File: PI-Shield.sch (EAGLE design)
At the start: 77 parts, among them IC1 PCF8574T, J10 T2I, J11 T2I, J12 T2I, J13 DF13-4P-1.25DSA, J14 DF13-4P-1.25DSA, J15 DF13-4P-1.25DSA, Q1 220mA/50V/3.5Ω, Q2 220mA/50V/3.5Ω, Q3 220mA/50V/3.5Ω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

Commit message: v2 Changes
Would like to formally apologize for the routing of the GPIO on the bottom of the board. It was necessary, unfortunately.
Changes: [Removed expander, added LED and Header Labels, really shitty routing.]
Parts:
- removed IC1: PCF8574T, micro-philips:PCF8574T
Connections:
- net 3V3: no longer IC1.VDD
- net GND: no longer IC1.A0, IC1.A1, IC1.A2, IC1.VSS
- net GPIO1: now also U$8.GPIO18; no longer IC1.P0
- net GPIO2: now also U$8.GPIO23; no longer IC1.P1
- net GPIO3: now also U$8.GPIO24; no longer IC1.P2
- net GPIO4: now also U$8.GPIO25; no longer IC1.P3
- net GPIO5: now also U$8.GPIO12; no longer IC1.P4
- net GPIO6: now also U$8.GPIO21; no longer IC1.P5
- net SCL: no longer IC1.SCL
- net SDA: no longer IC1.SDA
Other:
- note removed: "(address inputs)"
- note removed: "(used in place of the STM from last year)"
- note removed: "I/O Expander"
- note removed: "PCAL9554CPWJ"
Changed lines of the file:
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@@
 <part name="FRAME6" library="SparkFun-Aesthetics" library_urn="urn:adsk.eagle:library:507" deviceset="FRAME-A4L" device=""/>
 <part name="U3" library="ULN2003V12" deviceset="ULN2003V12" device=""/>
-<part name="IC1" library="micro-philips" library_urn="urn:adsk.eagle:library:290" deviceset="PCF8574" device="T" package3d_urn="urn:adsk.eagle:package:20172/1"/>
-<part name="SUPPLY1" library="supply2" library_urn="urn:adsk.eagle:library:372" deviceset="GND" device=""/>
 <part name="C15" library="SparkFun-Capacitors" library_urn="urn:adsk.eagle:library:510" deviceset="47UF-POLAR" device="-PANASONIC_D-35V-20%" package3d_urn="urn:adsk.eagle:package:37420/1" value="47uF"/>
 <part name="U$3" library="PI-SHIELD, Solenoid-Backplane" deviceset="6X_CONN" device=""/>
@@
 <wire x1="231.14" y1="149.86" x2="238.76" y2="149.86" width="0.1524" layer="91"/>
 <label x="233.68" y="149.86" size="1.778" layer="95"/>
+</segment>
+</net>
+<net name="GPIO1" class="0">
+<segment>
+<pinref part="U$8" gate="G$1" pin="GPIO18"/>
+<wire x1="25.4" y1="43.18" x2="20.32" y2="43.18" width="0.1524" layer="91"/>
+<label x="20.32" y="43.18" size="1.778" layer="95" rot="R180" xref="yes"/>
+</segment>
+</net>
+<net name="GPIO2" class="0">
+<segment>
+<pinref part="U$8" gate="G$1" pin="GPIO23"/>
+<wire x1="25.4" y1="53.34" x2="20.32" y2="53.34" width="0.1524" layer="91"/>
+<label x="20.32" y="53.34" size="1.778" layer="95" rot="R180" xref="yes"/>
+</segment>
+</net>
+<net name="GPIO3" class="0">
+<segment>
+<pinref part="U$8" gate="G$1" pin="GPIO24"/>
+<wire x1="25.4" y1="58.42" x2="20.32" y2="58.42" width="0.1524" layer="91"/>
+<label x="20.32" y="58.42" size="1.778" layer="95" rot="R180" xref="yes"/>
+</segment>
+</net>
+<net name="GPIO4" class="0">
+<segment>
+<pinref part="U$8" gate="G$1" pin="GPIO25"/>
+<wire x1="25.4" y1="68.58" x2="20.32" y2="68.58" width="0.1524" layer="91"/>
+<label x="20.32" y="68.58" size="1.778" layer="95" rot="R180" xref="yes"/>
+</segment>
+</net>
+<net name="GPIO5" class="0">
+<segment>
+<pinref part="U$8" gate="G$1" pin="GPIO12"/>
+<wire x1="25.4" y1="93.98" x2="20.32" y2="93.98" width="0.1524" layer="91"/>
+<label x="20.32" y="93.98" size="1.778" layer="95" rot="R180" xref="yes"/>
+</segment>
+</net>
+<net name="GPIO6" class="0">
+<segment>
+<pinref part="U$8" gate="G$1" pin="GPIO21"/>
+<wire x1="25.4" y1="114.3" x2="20.32" y2="114.3" width="0.1524" layer="91"/>
+<label x="20.32" y="114.3" size="1.778" layer="95" rot="R180" xref="yes"/>
 </segment>
 </net>
@@
 <text x="53.34" y="157.48" size="6.4516" layer="91">NPN Array</text>
 <text x="180.34" y="149.86" size="6.4516" layer="91">Connectors</text>
-<text x="142.24" y="86.36" size="1.778" layer="91">I/O Expander</text>
-<text x="137.16" y="43.18" size="1.778" layer="91">(used in place of the STM
-from last year)</text>
-<text x="139.7" y="86.36" size="1.778" layer="91">
-PCAL9554CPWJ
-</text>
-<text x="119.38" y="53.34" size="1.778" layer="91">(address inputs)</text>
 <text x="33.02" y="45.72" size="1.778" layer="91">decoupling cap for solenoids</text>
 <text x="33.02" y="48.26" size="1.778" layer="91">UZ476M035HEHTA</text>
@@
 </instance>
 <instance part="U3" gate="G$1" x="71.12" y="116.84" smashed="yes"/>
-<instance part="IC1" gate="G$1" x="147.32" y="68.58" smashed="yes"/>
-<instance part="SUPPLY1" gate="GND" x="114.3" y="50.8" smashed="yes">
-<attribute name="VALUE" x="112.395" y="47.625" size="1.778" layer="96"/>
-</instance>
 <instance part="C15" gate="G$1" x="68.58" y="48.26" smashed="yes">
 <attribute name="NAME" x="69.596" y="48.895" size="1.778" layer="95" font="vector"/>
@@
 </segment>
 <segment>
-<pinref part="IC1" gate="G$1" pin="VSS"/>
-<wire x1="160.02" y1="53.34" x2="172.72" y2="53.34" width="0.1524" layer="91"/>
-<label x="170.18" y="53.34" size="1.778" layer="95" align="bottom-right"/>
-</segment>
-<segment>
-<pinref part="IC1" gate="G$1" pin="A2"/>
-<wire x1="137.16" y1="58.42" x2="114.3" y2="58.42" width="0.1524" layer="91"/>
-<label x="127" y="58.42" size="1.778" layer="95"/>
-<pinref part="IC1" gate="G$1" pin="A1"/>
-<wire x1="137.16" y1="60.96" x2="114.3" y2="60.96" width="0.1524" layer="91"/>
-<label x="127" y="60.96" size="1.778" layer="95"/>
-<pinref part="IC1" gate="G$1" pin="A0"/>
-<wire x1="137.16" y1="63.5" x2="114.3" y2="63.5" width="0.1524" layer="91"/>
-<label x="127" y="63.5" size="1.778" layer="95"/>
-<wire x1="114.3" y1="63.5" x2="114.3" y2="60.96" width="0.1524" layer="91"/>
-<wire x1="114.3" y1="60.96" x2="114.3" y2="58.42" width="0.1524" layer="91"/>
-<junction x="114.3" y="60.96"/>
-<wire x1="114.3" y1="58.42" x2="114.3" y2="53.34" width="0.1524" layer="91"/>
-<junction x="114.3" y="58.42"/>
-<pinref part="SUPPLY1" gate="GND" pin="GND"/>
-</segment>
-<segment>
 <wire x1="68.58" y1="43.18" x2="68.58" y2="38.1" width="0.1524" layer="91"/>
 <label x="68.58" y="35.56" size="1.778" layer="95" rot="R90"/>
@@
 <pinref part="U3" gate="G$1" pin="IN1"/>
 </segment>
-<segment>
-<pinref part="IC1" gate="G$1" pin="P0"/>
-<wire x1="160.02" y1="76.2" x2="172.72" y2="76.2" width="0.1524" layer="91"/>
-<label x="170.18" y="76.2" size="1.778" layer="95" align="bottom-right"/>
-</segment>
 </net>
 <net name="GPIO6" class="0">
@@
 <pinref part="U3" gate="G$1" pin="IN6"/>
 </segment>
-<segment>
-<pinref part="IC1" gate="G$1" pin="P5"/>
-<wire x1="160.02" y1="63.5" x2="172.72" y2="63.5" width="0.1524" layer="91"/>
-<label x="170.18" y="63.5" size="1.778" layer="95" align="bottom-right"/>
-</segment>
 </net>
 <net name="GPIO5" class="0">
@@
 <pinref part="U3" gate="G$1" pin="IN5"/>
 </segment>
-<segment>
-<pinref part="IC1" gate="G$1" pin="P4"/>
-<wire x1="160.02" y1="66.04" x2="172.72" y2="66.04" width="0.1524" layer="91"/>
-<label x="170.18" y="66.04" size="1.778" layer="95" align="bottom-right"/>
-</segment>
 </net>
 <net name="GPIO4" class="0">
@@
 <pinref part="U3" gate="G$1" pin="IN4"/>
 </segment>
-<segment>
-<pinref part="IC1" gate="G$1" pin="P3"/>
-<wire x1="160.02" y1="68.58" x2="172.72" y2="68.58" width="0.1524" layer="91"/>
-<label x="170.18" y="68.58" size="1.778" layer="95" align="bottom-right"/>
-</segment>
 </net>
 <net name="GPIO3" class="0">
@@
 <pinref part="U3" gate="G$1" pin="IN3"/>
 </segment>
-<segment>
-<pinref part="IC1" gate="G$1" pin="P2"/>
-<wire x1="160.02" y1="71.12" x2="172.72" y2="71.12" width="0.1524" layer="91"/>
-<label x="170.18" y="71.12" size="1.778" layer="95" align="bottom-right"/>
-</segment>
 </net>
 <net name="GPIO2" class="0">
@@
 <pinref part="U3" gate="G$1" pin="IN2"/>
 </segment>
-<segment>
-<pinref part="IC1" gate="G$1" pin="P1"/>
-<wire x1="160.02" y1="73.66" x2="172.72" y2="73.66" width="0.1524" layer="91"/>
-<label x="170.18" y="73.66" size="1.778" layer="95" align="bottom-right"/>
-</segment>
-</net>
-<net name="SCL" class="0">
-<segment>
-<pinref part="IC1" gate="G$1" pin="SCL"/>
-<wire x1="137.16" y1="68.58" x2="124.46" y2="68.58" width="0.1524" layer="91"/>
-<label x="127" y="68.58" size="1.778" layer="95"/>
-</segment>
-</net>
-<net name="SDA" class="0">
-<segment>
-<pinref part="IC1" gate="G$1" pin="SDA"/>
-<wire x1="137.16" y1="71.12" x2="124.46" y2="71.12" width="0.1524" layer="91"/>
-<label x="127" y="71.12" size="1.778" layer="95"/>
-</segment>
 </net>
 <net name="5V" class="2">
@@
 </net>
 <net name="3V3" class="3">
-<segment>
-<pinref part="IC1" gate="G$1" pin="VDD"/>
-<wire x1="160.02" y1="81.28" x2="172.72" y2="81.28" width="0.1524" layer="91"/>
-<label x="170.18" y="81.28" size="1.778" layer="95" align="bottom-right"/>
-</segment>
 <segment>
 <wire x1="182.88" y1="125.73" x2="195.58" y2="125.73" width="0.1524" layer="91"/>
@@
 packages will not be understood (or retained) with this version.
 </note>
-<note version="9.0" severity="warning">
-Since Version 9.0, EAGLE supports the align property for labels.
-Labels in schematic will not be understood with this version. Update EAGLE to the latest version
-for full support of labels.
-</note>
 </compatibility>

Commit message: Adjusted some labels, fixed minor errors
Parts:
- removed U$3: 6X_CONN, PI-SHIELD, Solenoid-Backplane:6X_CONN
- added U$9: 7X_CONN, PI-SHIELD, Solenoid-Backplane:7X_CONN
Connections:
- net 12V: now also U$9.13, U$9.15; no longer U$3.13, U$3.15
- net 3V3: now also U$9.23; no longer U$3.23
- net 5V: now also U$9.19; no longer U$3.19
- net CAN_H: now also U$9.1
- net CAN_L: now also U$9.2
- net GND: now also U$9.17, U$9.21; no longer U$3.17, U$3.21
- net SOL1_1: now also U$9.14; no longer U$3.14
- net SOL2_1: now also U$9.16; no longer U$3.16
- net SOL3_1: now also U$9.18; no longer U$3.18
- net SOL4_1: now also U$9.20; no longer U$3.20
- net SOL5_1: now also U$9.22; no longer U$3.22
- net SOL6_1: now also U$9.24; no longer U$3.24
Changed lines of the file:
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@@
 <?xml version="1.0" encoding="utf-8"?>
 <!DOCTYPE eagle SYSTEM "eagle.dtd">
-<eagle version="9.6.2">
+<eagle version="9.5.0">
 <drawing>
 <settings>
@@
 <setting verticaltext="up"/>
 </settings>
-<grid distance="0.1" unitdist="inch" unit="inch" style="lines" multiple="1" display="no" altdistance="0.01" altunitdist="inch" altunit="inch"/>
+<grid distance="50" unitdist="mil" unit="mil" style="lines" multiple="1" display="no" altdistance="0.01" altunitdist="inch" altunit="inch"/>
 <layers>
 <layer number="1" name="Top" color="4" fill="1" visible="no" active="no"/>
@@
 <part name="U3" library="ULN2003V12" deviceset="ULN2003V12" device=""/>
 <part name="C15" library="SparkFun-Capacitors" library_urn="urn:adsk.eagle:library:510" deviceset="47UF-POLAR" device="-PANASONIC_D-35V-20%" package3d_urn="urn:adsk.eagle:package:37420/1" value="47uF"/>
-<part name="U$3" library="PI-SHIELD, Solenoid-Backplane" deviceset="6X_CONN" device=""/>
+<part name="U$9" library="PI-SHIELD, Solenoid-Backplane" deviceset="7X_CONN" device=""/>
 </parts>
 <sheets>
@@
 <segment>
 <pinref part="U$8" gate="G$1" pin="GPIO18"/>
-<wire x1="25.4" y1="43.18" x2="20.32" y2="43.18" width="0.1524" layer="91"/>
-<label x="20.32" y="43.18" size="1.778" layer="95" rot="R180" xref="yes"/>
+<wire x1="25.4" y1="43.18" x2="19.05" y2="43.18" width="0.1524" layer="91"/>
+<label x="19.05" y="43.18" size="1.778" layer="95" rot="R180" xref="yes"/>
 </segment>
 </net>
@@
 <segment>
 <pinref part="U$8" gate="G$1" pin="GPIO23"/>
-<wire x1="25.4" y1="53.34" x2="20.32" y2="53.34" width="0.1524" layer="91"/>
-<label x="20.32" y="53.34" size="1.778" layer="95" rot="R180" xref="yes"/>
+<wire x1="25.4" y1="53.34" x2="19.05" y2="53.34" width="0.1524" layer="91"/>
+<label x="19.05" y="53.34" size="1.778" layer="95" rot="R180" xref="yes"/>
 </segment>
 </net>
@@
 <segment>
 <pinref part="U$8" gate="G$1" pin="GPIO12"/>
-<wire x1="25.4" y1="93.98" x2="20.32" y2="93.98" width="0.1524" layer="91"/>
-<label x="20.32" y="93.98" size="1.778" layer="95" rot="R180" xref="yes"/>
+<wire x1="25.4" y1="93.98" x2="19.05" y2="93.98" width="0.1524" layer="91"/>
+<label x="19.05" y="93.98" size="1.778" layer="95" rot="R180" xref="yes"/>
 </segment>
 </net>
@@
 <attribute name="VALUE" x="69.596" y="44.069" size="1.778" layer="96" font="vector"/>
 </instance>
-<instance part="U$3" gate="G$1" x="203.2" y="132.08" smashed="yes"/>
+<instance part="U$9" gate="G$1" x="203.2" y="132.08" smashed="yes">
+<attribute name="NAME" x="198.755" y="141.605" size="1.778" layer="95" font="vector"/>
+</instance>
 </instances>
 <busses>
@@
 <wire x1="195.58" y1="133.35" x2="182.88" y2="133.35" width="0.1524" layer="91"/>
 <label x="185.42" y="133.35" size="1.778" layer="95"/>
-<pinref part="U$3" gate="G$1" pin="17"/>
+<pinref part="U$9" gate="G$1" pin="17"/>
 </segment>
 <segment>
 <wire x1="195.58" y1="128.27" x2="182.88" y2="128.27" width="0.1524" layer="91"/>
 <label x="185.42" y="128.27" size="1.778" layer="95"/>
-<pinref part="U$3" gate="G$1" pin="21"/>
+<pinref part="U$9" gate="G$1" pin="21"/>
 </segment>
 </net>
@@
 <wire x1="195.58" y1="138.43" x2="182.88" y2="138.43" width="0.1524" layer="91"/>
 <label x="185.42" y="138.43" size="1.778" layer="95"/>
-<pinref part="U$3" gate="G$1" pin="13"/>
+<pinref part="U$9" gate="G$1" pin="13"/>
 </segment>
 <segment>
 <wire x1="195.58" y1="135.89" x2="182.88" y2="135.89" width="0.1524" layer="91"/>
 <label x="185.42" y="135.89" size="1.778" layer="95"/>
-<pinref part="U$3" gate="G$1" pin="15"/>
+<pinref part="U$9" gate="G$1" pin="15"/>
 </segment>
 </net>
@@
 <wire x1="223.52" y1="138.43" x2="210.82" y2="138.43" width="0.1524" layer="91"/>
 <label x="213.36" y="138.43" size="1.778" layer="95"/>
-<pinref part="U$3" gate="G$1" pin="14"/>
+<pinref part="U$9" gate="G$1" pin="14"/>
 </segment>
 </net>
@@
 <wire x1="223.52" y1="135.89" x2="210.82" y2="135.89" width="0.1524" layer="91"/>
 <label x="213.36" y="135.89" size="1.778" layer="95"/>
-<pinref part="U$3" gate="G$1" pin="16"/>
+<pinref part="U$9" gate="G$1" pin="16"/>
 </segment>
 </net>
@@
 <wire x1="223.52" y1="133.35" x2="210.82" y2="133.35" width="0.1524" layer="91"/>
 <label x="213.36" y="133.35" size="1.778" layer="95"/>
-<pinref part="U$3" gate="G$1" pin="18"/>
+<pinref part="U$9" gate="G$1" pin="18"/>
 </segment>
 </net>
@@
 <wire x1="223.52" y1="130.81" x2="210.82" y2="130.81" width="0.1524" layer="91"/>
 <label x="213.36" y="130.81" size="1.778" layer="95"/>
-<pinref part="U$3" gate="G$1" pin="20"/>
+<pinref part="U$9" gate="G$1" pin="20"/>
 </segment>
 </net>
@@
 <wire x1="223.52" y1="128.27" x2="210.82" y2="128.27" width="0.1524" layer="91"/>
 <label x="213.36" y="128.27" size="1.778" layer="95"/>
-<pinref part="U$3" gate="G$1" pin="22"/>
+<pinref part="U$9" gate="G$1" pin="22"/>
 </segment>
 </net>
@@
 <wire x1="223.52" y1="125.73" x2="210.82" y2="125.73" width="0.1524" layer="91"/>
 <label x="213.36" y="125.73" size="1.778" layer="95"/>
-<pinref part="U$3" gate="G$1" pin="24"/>
+<pinref part="U$9" gate="G$1" pin="24"/>
 </segment>
 </net>
@@
 <segment>
 <wire x1="195.58" y1="130.81" x2="182.88" y2="130.81" width="0.1524" layer="91"/>
-<pinref part="U$3" gate="G$1" pin="19"/>
 <label x="185.42" y="130.81" size="1.778" layer="95"/>
+<pinref part="U$9" gate="G$1" pin="19"/>
 </segment>
 </net>
@@
 <segment>
 <wire x1="182.88" y1="125.73" x2="195.58" y2="125.73" width="0.1524" layer="91"/>
-<pinref part="U$3" gate="G$1" pin="23"/>
 <label x="185.42" y="125.73" size="1.778" layer="95"/>
-</segment>
-</net>
+<pinref part="U$9" gate="G$1" pin="23"/>
+</segment>
+</net>
+<net name="CAN_L" class="1">
+<segment>
+<pinref part="U$9" gate="G$1" pin="2"/>
+<wire x1="195.58" y1="123.19" x2="182.88" y2="123.19" width="0.1524" layer="91"/>
+<label x="185.42" y="123.19" size="1.778" layer="95"/>
+</segment>
+</net>
+<net name="CAN_H" class="1">
+<segment>
+<pinref part="U$9" gate="G$1" pin="1"/>
+<wire x1="210.82" y1="123.19" x2="223.52" y2="123.19" width="0.1524" layer="91"/>
+<label x="213.36" y="123.19" size="1.778" layer="95"/>
+</segment>
+</net>

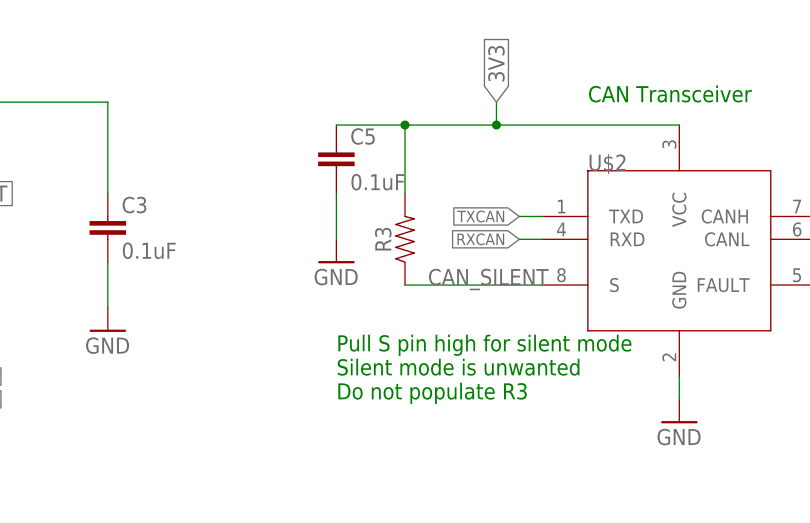
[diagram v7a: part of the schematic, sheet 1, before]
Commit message: Replaced R3 with Jumper, exported STEP
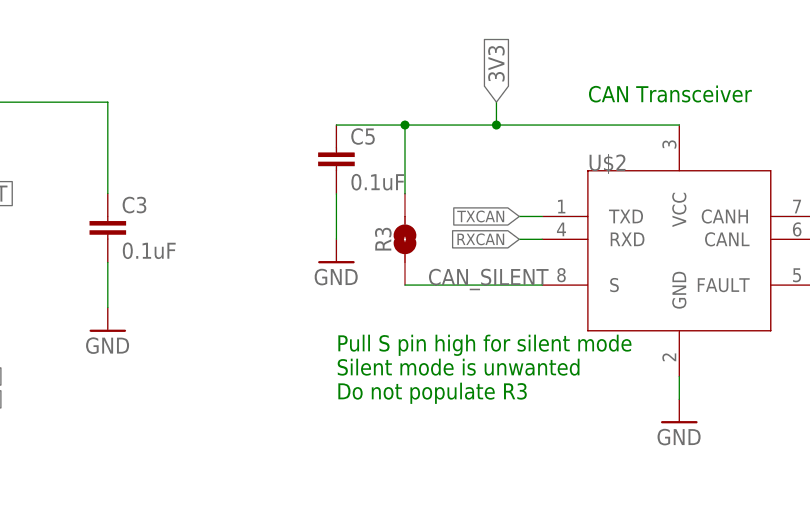
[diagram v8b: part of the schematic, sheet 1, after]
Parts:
- R3: value (none) -> JUMPER-SMT_2_NO_SILK; device SparkFun-Resistors:RESISTOR0603 -> SparkFun-Jumpers:JUMPER-SMT_2_NO_SILK
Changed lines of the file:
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@@
 <part name="GND10" library="supply1" library_urn="urn:adsk.eagle:library:371" deviceset="GND" device=""/>
 <part name="U$1" library="STM and CAN parts" deviceset="MCP2515" device=""/>
-<part name="R3" library="SparkFun-Resistors" library_urn="urn:adsk.eagle:library:532" deviceset="RESISTOR" device="0603" package3d_urn="urn:adsk.eagle:package:39650/1" value=" "/>
+<part name="R3" library="SparkFun-Jumpers" library_urn="urn:adsk.eagle:library:528" deviceset="JUMPER-SMT_2_NO" device="_SILK" package3d_urn="urn:adsk.eagle:package:39279/1" value="JUMPER-SMT_2_NO_SILK"/>
 <part name="C5" library="SparkFun-Capacitors" library_urn="urn:adsk.eagle:library:510" deviceset="22NF/22,000PF" device="-0603-50V-10%" package3d_urn="urn:adsk.eagle:package:37414/1" value="0.1uF"/>
 <part name="GND5" library="supply1" library_urn="urn:adsk.eagle:library:371" deviceset="GND" device=""/>
@@
 <instance part="R3" gate="G$1" x="116.84" y="144.78" smashed="yes" rot="R90">
 <attribute name="NAME" x="115.316" y="144.78" size="1.778" layer="95" font="vector" rot="R90" align="bottom-center"/>
-<attribute name="VALUE" x="118.364" y="144.78" size="1.778" layer="96" font="vector" rot="R90" align="top-center"/>
 </instance>
 <instance part="C5" gate="G$1" x="109.22" y="152.4" smashed="yes">
